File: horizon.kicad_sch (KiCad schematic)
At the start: 72 parts, among them IC1 A3909, J1 Micro_SD_Card_Det1, J10 Conn_01x02_Pin, J3 Conn_01x02, J4 Conn_01x02, J5 Conn_01x02, J6 Conn_01x02, J9 USB_C_Receptacle_USB2.0_16P, Q2 DMG2301L, U1 MMCU, U12 TPS63061, U13 LTC4412xS6, U14 TPS61092, U15 AP2112K-3.3, U16 TPS61092, U2 IMU, U3 NMCU, U4 TMCU, U5 LPS22HB, U6 GPS, U7 SX1276, U8 NAND, U9 TPS82130

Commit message: data + bootloader pins
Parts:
- removed J4: Conn_01x02, symbol Connector_Generic:Conn_01x02
- added J2, J7, J8: Conn_02x03_Counter_Clockwise, symbol Connector_Generic:Conn_02x03_Counter_Clockwise
- added SW1, SW2: SW_Rotary_1x3_MP, symbol Switch:SW_Rotary_1x3_MP
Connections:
- net +3.3V: now also J2.1 (Pin_1), J7.1 (Pin_1), J8.1 (Pin_1)
- net DMCU-1 SCL: no longer U1.37 (D19/A5/SCL0/TOUCH), U4.44 (PA23)
- net DMCU-1 SDA: no longer U1.38 (D18/A4/SDA0/TOUCH), U4.43 (PA22)
- net GND: now also J2.3 (Pin_3), J7.3 (Pin_3), J8.3 (Pin_3)
- net at D6.2 (I/O1), J9.A6 (D+), J9.B6 (D+)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: now also SW1.4
- net at D6.3 (I/O2), J9.A7 (D-), J9.B7 (D-)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: now also SW2.4
- net SWCLK MMCU: now reaches U1.22 (PTA0)
- net SWCLK MMCU: now also J2.2 (Pin_2)
- net SWDIO MMCU: now reaches U1.23 (PTA1)
- net SWDIO MMCU: now also J2.5 (Pin_5)
- net nRESET MMCU: now reaches U1.34 (RESET)
- net nRESET MMCU: now also J2.4 (Pin_4)
- net nRESET DMCU-2: now reaches U4.52 (~{RESET})
- net nRESET DMCU-2: now also J8.4 (Pin_4)
- net SWCLK DMCU-2: now reaches U4.57 (PA30)
- net SWCLK DMCU-2: now also J8.2 (Pin_2)
- net SWDIO DMCU-2: now reaches U4.58 (PA31)
- net SWDIO DMCU-2: now also J8.5 (Pin_5)
- net nRESET DMCU-1: now reaches U3.52 (~{RESET})
- net nRESET DMCU-1: now also J7.4 (Pin_4)
- net SWCLK DMCU-1: now reaches U3.57 (PA30)
- net SWCLK DMCU-1: now also J7.2 (Pin_2)
- net SWDIO DMCU-1: now reaches U3.58 (PA31)
- net SWDIO DMCU-1: now also J7.5 (Pin_5)
- new net D+ DMCU-1: SW1.2
- new net D+ DMCU-2: SW1.3
- new net D+ MMCU: SW1.1
- new net D- DMCU-1: SW2.2
- new net D- DMCU-2: SW2.3
- new net D- MMCU: SW2.1
- new net DMCU-2 SCL: U4.44 (PA23)
- new net DMCU-2 SDA: U4.43 (PA22)
- new net MMCU SCL: U1.37 (D19/A5/SCL0/TOUCH)
- new net MMCU SDA: U1.38 (D18/A4/SDA0/TOUCH)
- no-connect marks 2 -> 5
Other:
- moved on the sheet: C10, C26, C28, C29, C30, C31, C32, C33, C34, C35, C36, C37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

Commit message: switch for programming, data lines
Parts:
- removed J3, J5, J6: Conn_01x02, symbol Connector_Generic:Conn_01x02
- added C1, C3, C4: 100nF, symbol Device:C
- added C2: 10uF, symbol Device:C
- added L5: SLF7055T-6R8N2R8-3PF, Inductor_SMD:L_7.3x7.3_H4.5, symbol SLF7055T-6R8N2R8-3PF[1]:SLF7055T-6R8N2R8-3PF
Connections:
- net +3.3V: now also U3.21 (VDDIO), U3.34 (VDDIO), U3.48 (VDDIO), U3.56 (VDDIN), C3.2, C4.2, L5.1
- net D+ DMCU-1: now also U3.45 (PA24)
- net D+ DMCU-2: now also U4.45 (PA24)
- net D+ MMCU: now also U1.5 (USB-P)
- net D- DMCU-1: now also U3.46 (PA25)
- net D- DMCU-2: now also U4.46 (PA25)
- net D- MMCU: now also U1.6 (USB-M)
- net GND: now also U3.55 (VDDCORE), U3.7 (GNDANA), C1.2, C2.2, C3.1, C4.1
- net at U3.8 (VDDANA): now also C1.1, C2.1, L5.2
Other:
- note removed: "D+ and D- pins"
- moved on the sheet: IC1, J2, J7, J8, U1, U2, U3, U4, U6, U7, U8

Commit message: mcu
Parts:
- added C11, C12, C13, C9: C, symbol Device:C
- added C5, C6, C8: 100nF, symbol Device:C
- added C7: 10uF, symbol Device:C
- added FL3, FL4: Choke_CommonMode_PulseElectronics_PH9455x105NL, Inductor_THT:L_CommonMode_PulseElectronics_PH9455x105NL_1, symbol Filter:Choke_CommonMode_PulseElectronics_PH9455x105NL
- added L6: SLF7055T-6R8N2R8-3PF, Inductor_SMD:L_7.3x7.3_H4.5, symbol SLF7055T-6R8N2R8-3PF[1]:SLF7055T-6R8N2R8-3PF
- added R3, R4, R5: 10k, symbol Device:R
- added R6, R7: 4.7k, symbol Device:R
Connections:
- net DMCU-1 SCL is gone; now on net sda: U3.44 (PA23)
- net DMCU-1 SDA is gone; now on net scl: U3.43 (PA22)
- net DMCU-2 SCL is gone; now on net sda: U4.44 (PA23)
- net DMCU-2 SDA is gone; now on net scl: U4.43 (PA22)
- net +3.3V: now also U1.13 (VCCA), U1.3 (VCC), U1.30 (VCC), U1.48 (VCC), U1.7 (VOUT3V3), U1.8 (VREGIN), U4.21 (VDDIO), U4.34 (VDDIO), U4.48 (VDDIO), U4.56 (VDDIN), C11.1, C12.1, C13.1, C5.2, C6.2, C9.1, L6.1, R3.2, R4.2, R5.2, R6.1, R7.1
- net GND: now also U4.55 (VDDCORE), C11.2, C12.2, C13.2, C5.1, C6.1, C7.2, C8.2, C9.2
- net nRESET DMCU-1: now also R3.1
- net nRESET DMCU-2: now also R5.1
- net nRESET MMCU: now also R4.1
- net at U13.4 (STAT): now also U9.1 (EN)
- net scl: now reaches U1.55 (D29/A18/SCL1)
- net scl: now also R6.2
- net sda: now reaches U1.56 (D30/A19/SDA1)
- net sda: now also R7.2
- net at D6.3 (I/O2), J9.A7 (D-), J9.B7 (D-)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: now also FL3.2, FL4.2; no longer SW2.4
- net at C32.1, D20.1 (K), U9.2 (VIN): no longer U9.1 (EN)
- net at U4.8 (VDDANA): now also C7.1, C8.1, L6.2
- net at D6.2 (I/O1), J9.A6 (D+), J9.B6 (D+)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: now also FL3.1, FL4.1; no longer SW1.4
- net MMCU SCL: no longer names the net of U1.37 (D19/A5/SCL0/TOUCH)
- net MMCU SDA: no longer names the net of U1.38 (D18/A4/SDA0/TOUCH)
- new net: FL3.3, FL4.3, SW2.4
- new net: FL3.4, FL4.4, SW1.4
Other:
- moved on the sheet: C1, C10, C2, C26, C3, C4, D23, D5, D6, J2, J7, J8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

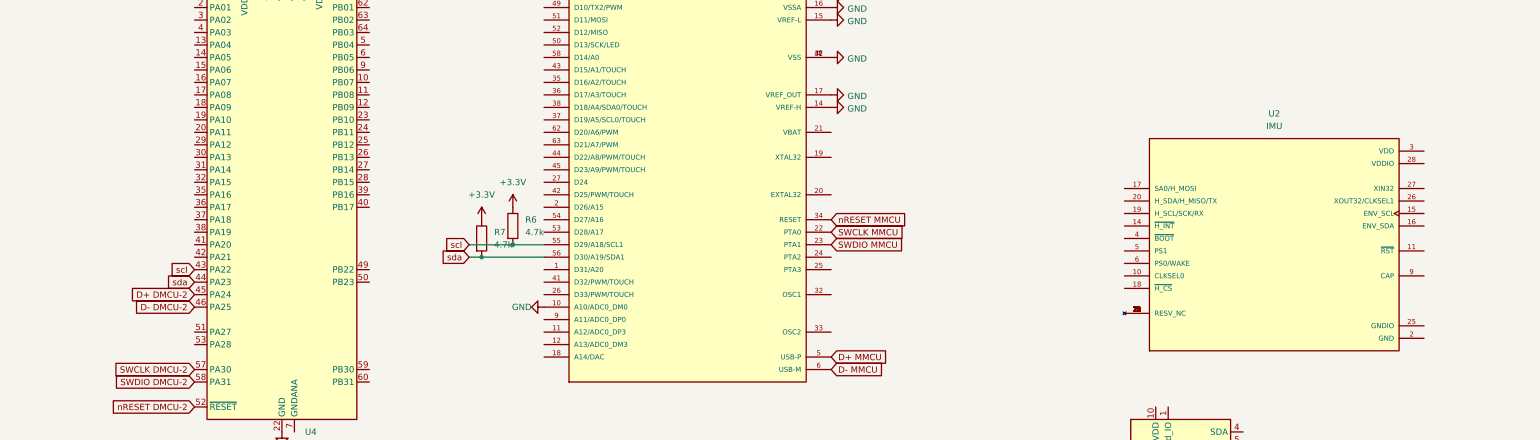
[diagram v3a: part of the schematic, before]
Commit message: Added IMU Schematics and connected it to TMU via SPI
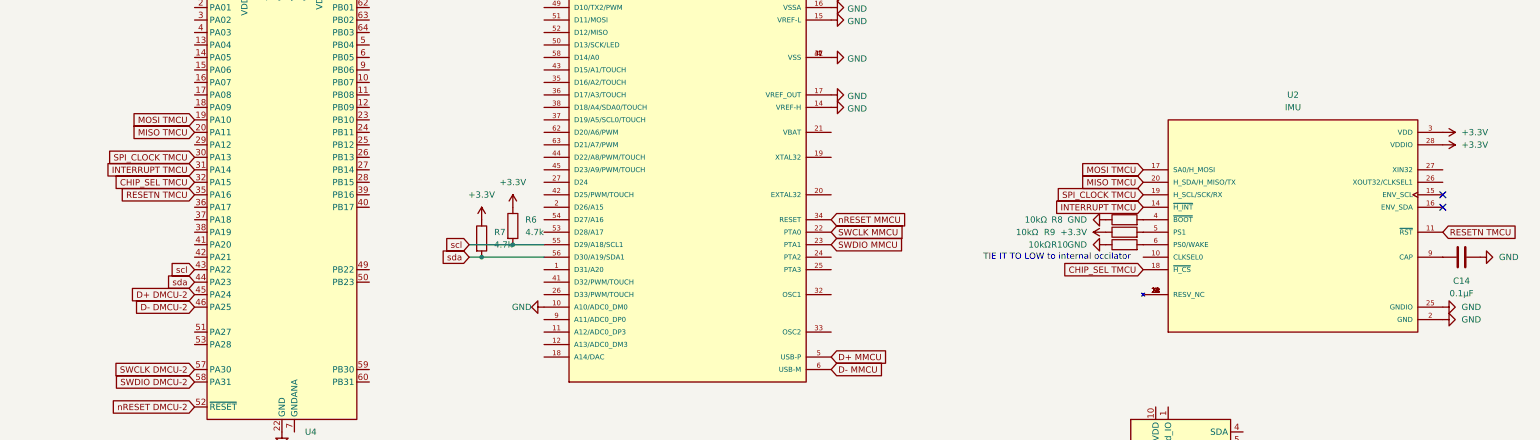
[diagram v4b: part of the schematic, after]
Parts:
- added C14: 0.1µF, symbol Device:C
- added R10, R8, R9: 10kΩ, symbol Device:R
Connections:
- net +3.3V: now also U2.28 (VDDIO), U2.3 (VDD), R9.1
- net GND: now also U2.2 (GND), U2.25 (GNDIO), C14.1, R10.1, R8.1
- net MOSI TMCU: now reaches U4.19 (PA10)
- net MOSI TMCU: now also U2.17 (SA0/H_MOSI)
- net MISO TMCU: now reaches U4.20 (PA11)
- net MISO TMCU: now also U2.20 (H_SDA/H_MISO/TX)
- net SPI_CLOCK TMCU: now reaches U4.30 (PA13)
- net SPI_CLOCK TMCU: now also U2.19 (H_SCL/SCK/RX)
- net INTERRUPT TMCU: now reaches U4.31 (PA14)
- net INTERRUPT TMCU: now also U2.14 (~{H_INT})
- net CHIP_SEL TMCU: now reaches U4.32 (PA15)
- net CHIP_SEL TMCU: now also U2.18 (~{H_CS})
- net RESETN TMCU: now reaches U4.35 (PA16)
- net RESETN TMCU: now also U2.11 (~{RST})
- net at U2.4 (~{BOOT}): now also R8.2
- net at U2.5 (PS1): now also R9.2
- net at U2.6 (PS0/WAKE): now also R10.2
- net at U2.9 (CAP): now also C14.2
- no-connect marks 5 -> 7
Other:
- note added: "TIE IT TO LOW to internal occilator"
- moved on the sheet: U2

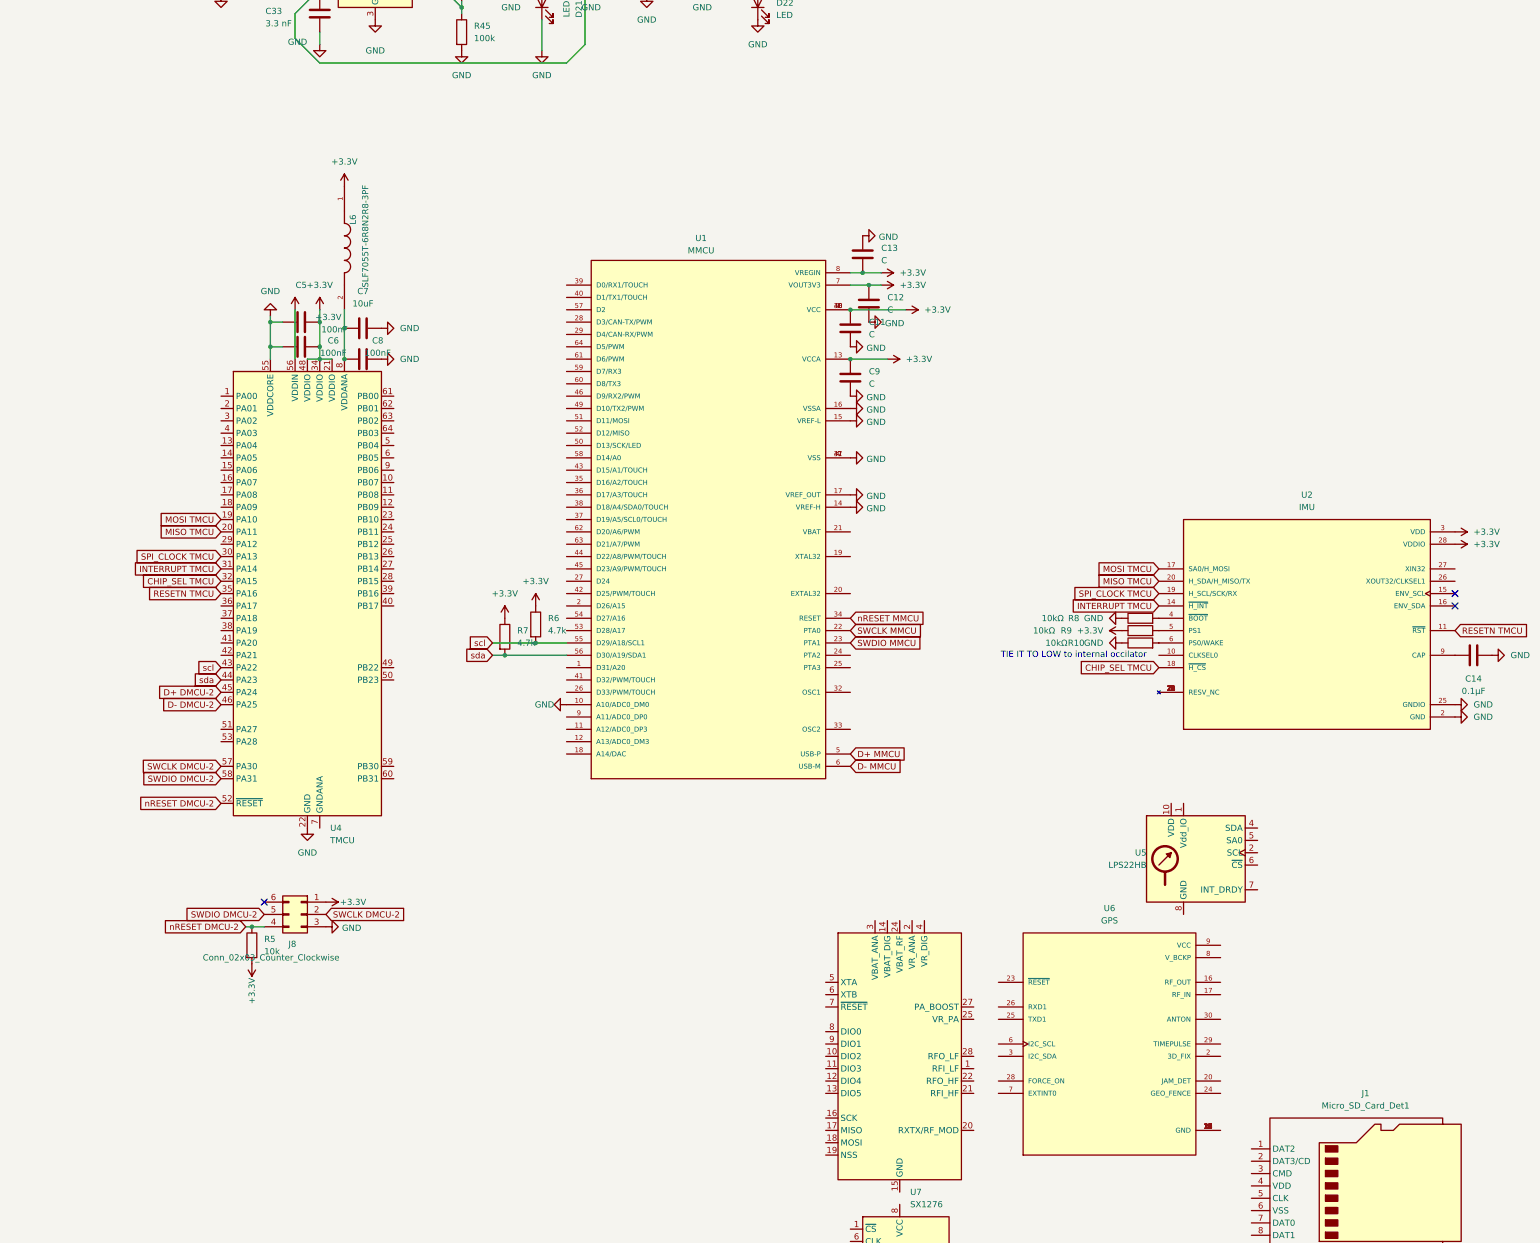
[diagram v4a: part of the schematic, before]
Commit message: Added like 1/3 of the GPS Schematic
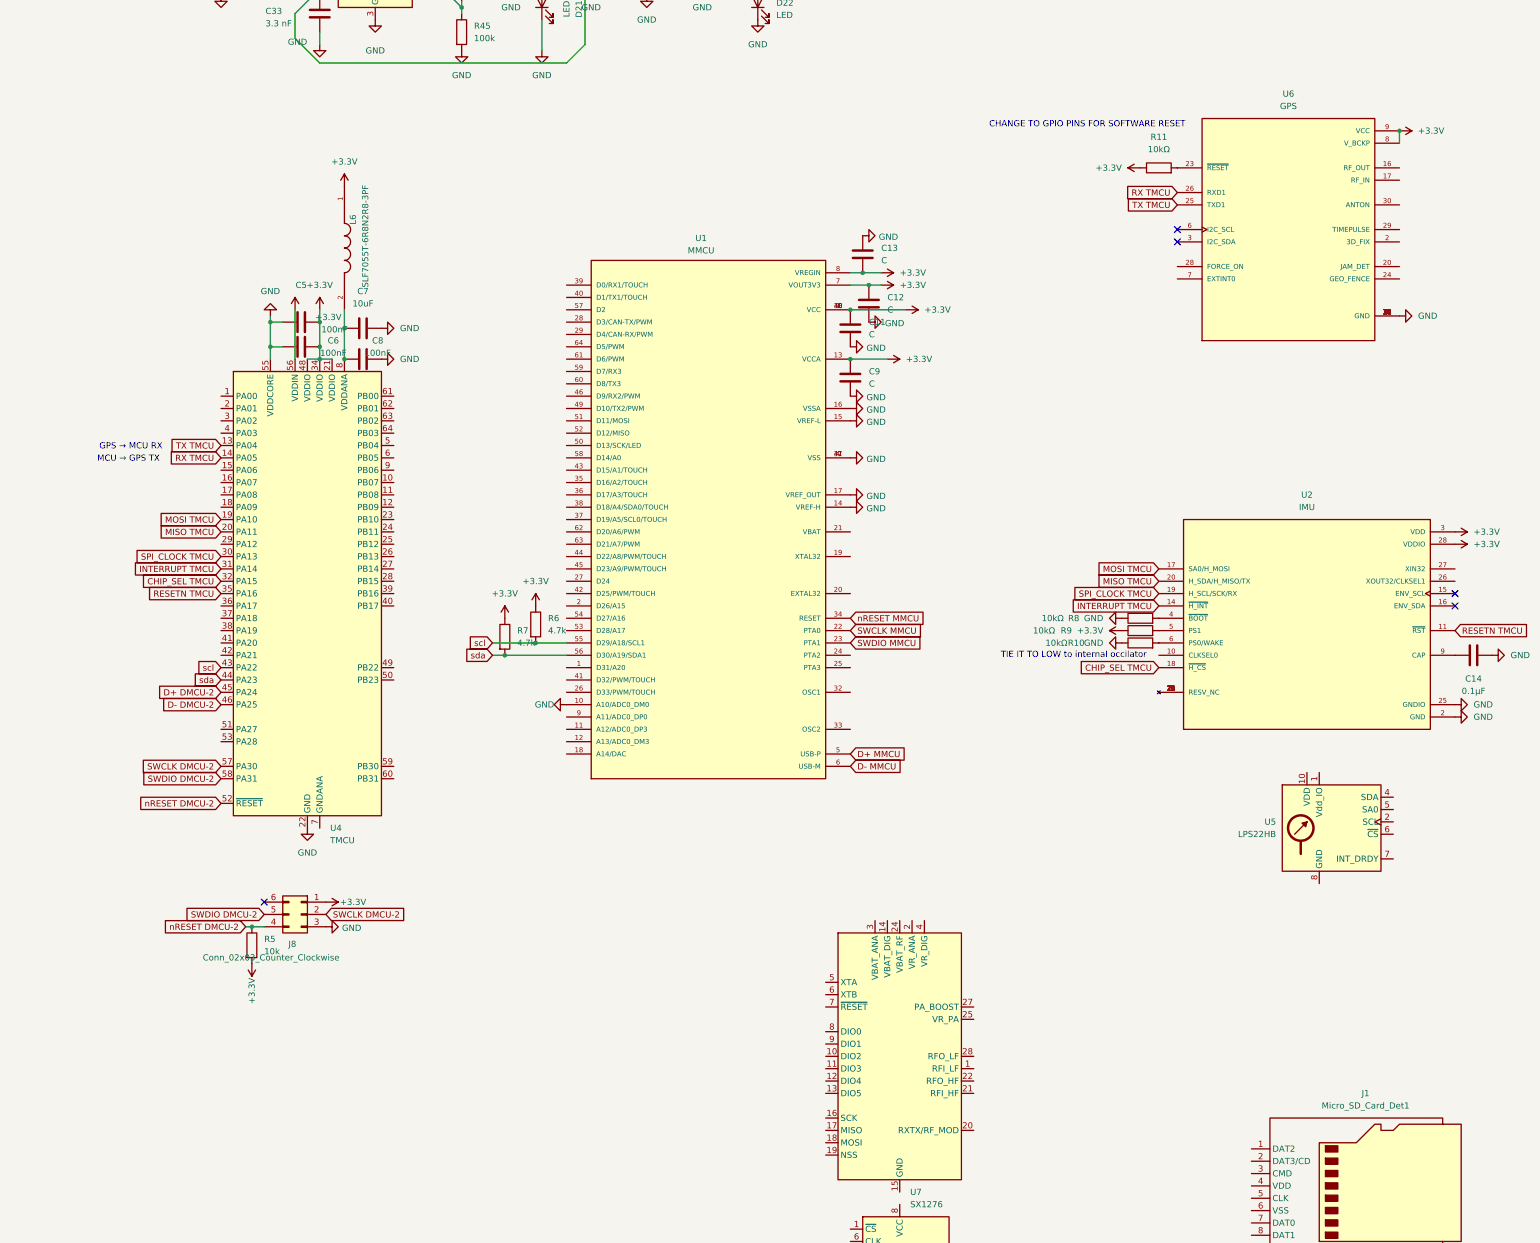
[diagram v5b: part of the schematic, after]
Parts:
- added R11: 10kΩ, symbol Device:R
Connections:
- net +3.3V: now also U6.8 (V_BCKP), U6.9 (VCC), R11.1
- net GND: now also U6.10 (GND), U6.11 (GND), U6.12 (GND), U6.13 (GND), U6.14 (GND), U6.15 (GND), U6.18 (GND), U6.19 (GND), U6.21 (GND), U6.22 (GND), U6.27 (GND), U6.31 (GND), U6.4 (GND), U6.5 (GND)
- net TX TMCU: now reaches U4.13 (PA04)
- net TX TMCU: now also U6.25 (TXD1)
- net RX TMCU: now reaches U4.14 (PA05)
- net RX TMCU: now also U6.26 (RXD1)
- net at U6.23 (~{RESET}): now also R11.2
- no-connect marks 7 -> 9
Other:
- note added: "CHANGE TO GPIO PINS FOR SOFTWARE RESET"
- note added: "GPS → MCU RX"
- note added: "MCU → GPS TX"
- moved on the sheet: U6

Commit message: Baro schematics done
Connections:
- net +3.3V: now also U5.1 (Vdd_IO), U5.10 (VDD)
- net CHIP_SEL TMCU: now also U5.2 (SCL); no longer U2.18 (~{H_CS}), U4.32 (PA15)
- net GND: now also U5.3 (GND), U5.8 (GND), U5.9 (GND)
- net MISO TMCU: now also U5.5 (SA0)
- net MOSI TMCU: now also U5.4 (SDA)
- net CHIP_SEL_BARO TMCU: now reaches U4.63 (PB02)
- net CHIP_SEL_BARO TMCU: now also U5.6 (~{CS})
- net Baro_int TMCU: now reaches U5.7 (INT_DRDY)
- new net CHIP_SEL_IMU TMCU: U2.18 (~{H_CS}), U4.32 (PA15)
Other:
- note added: "Pull low to talk to IMU"
- note added: "Set low to talk to BARO"

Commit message: SD Card is Done
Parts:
- added C15: 0.1 µF, symbol Device:C
- added R12, R13: 10kΩ, symbol Device:R
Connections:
- net +3.3V: now also J1.4 (VDD), C15.1
- net GND: now also J1.10 (SHIELD), J1.6 (VSS), U8.4 (GND)
- net CS_SD MMCU: now reaches U1.42 (D25/PWM/TOUCH)
- net CS_SD MMCU: now also J1.2 (DAT3/CD)
- net CS_NAND MMCU: now reaches U1.43 (D15/A1/TOUCH)
- net CS_NAND MMCU: now also U8.1 (~{CS})
- net NAND_MOSI MMCU: now reaches U1.51 (D11/MOSI)
- net NAND_MOSI MMCU: now also U8.5 (DI/IO_{0})
- net NAND_MISO MMCU: now reaches U1.52 (D12/MISO)
- net NAND_MISO MMCU: now also U8.2 (DO/IO_{1})
- net  SPI0_SCK MMCU: now reaches U1.53 (D28/A17)
- net  SPI0_SCK MMCU: now also U8.6 (CLK)
- net at U8.3 (~{WP}/IO_{2}): now also R12.2
- net at U8.7 (~{HOLD}/~{RESET}/IO_{3}): now also R13.2
- net at U8.8 (VCC): now also C15.2
- net MOSI_SD MMCU: now reaches J1.3 (CMD)
- net SCK_SD MMCU: now reaches J1.5 (CLK)
- net MISO_SD MMCU: now reaches J1.7 (DAT0)
- new net: R12.1, R13.1
- no-connect marks 9 -> 12
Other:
- moved on the sheet: C5, C6, C7, C8, IC1, J1, L6, R6, R7, U4, U8

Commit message: Some text additions
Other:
- note added: "For NAND and SD"
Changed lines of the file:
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@@
 	(generator_version "9.0")
 	(paper "A4")
+	(text "For NAND and SD"
+		(exclude_from_sim no)
+		(at 293.878 157.48 0)
+		(effects
+			(font
+				(size 1.27 1.27)
+			)
+		)
+	)
 	(text "CHANGE TO GPIO PINS FOR SOFTWARE RESET"
 		(exclude_from_sim no)
@@
 		)
 	)
+	(text "For NAND and SD"
+		(exclude_from_sim no)
+		(at 311.912 197.612 0)
+		(effects
+			(font
+				(size 1.27 1.27)
+			)
+		)
+	)
 	(text "MCU → GPS TX"
 		(exclude_from_sim no)
@@
 		(effects
 			(font
+				(size 1.27 1.27)
+			)
+		)
+	)
+	(text "For NAND and SD"
+		(exclude_from_sim no)
+		(at 293.37 160.274 0)
+		(effects
+			(font
